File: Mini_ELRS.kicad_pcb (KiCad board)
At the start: 4 copper layers, 27.9 x 26.9 mm, 24 parts, among them J1 Conn_01x06, J2 Conn_01x06, J3 Conn_01x06, SW1 SW_Push, U1 ESP32-PICO-D4, U2 TC2014-3.3VxCTTR, U3 SX1280IMLTRT, Y1 Crystal_GND24_Small

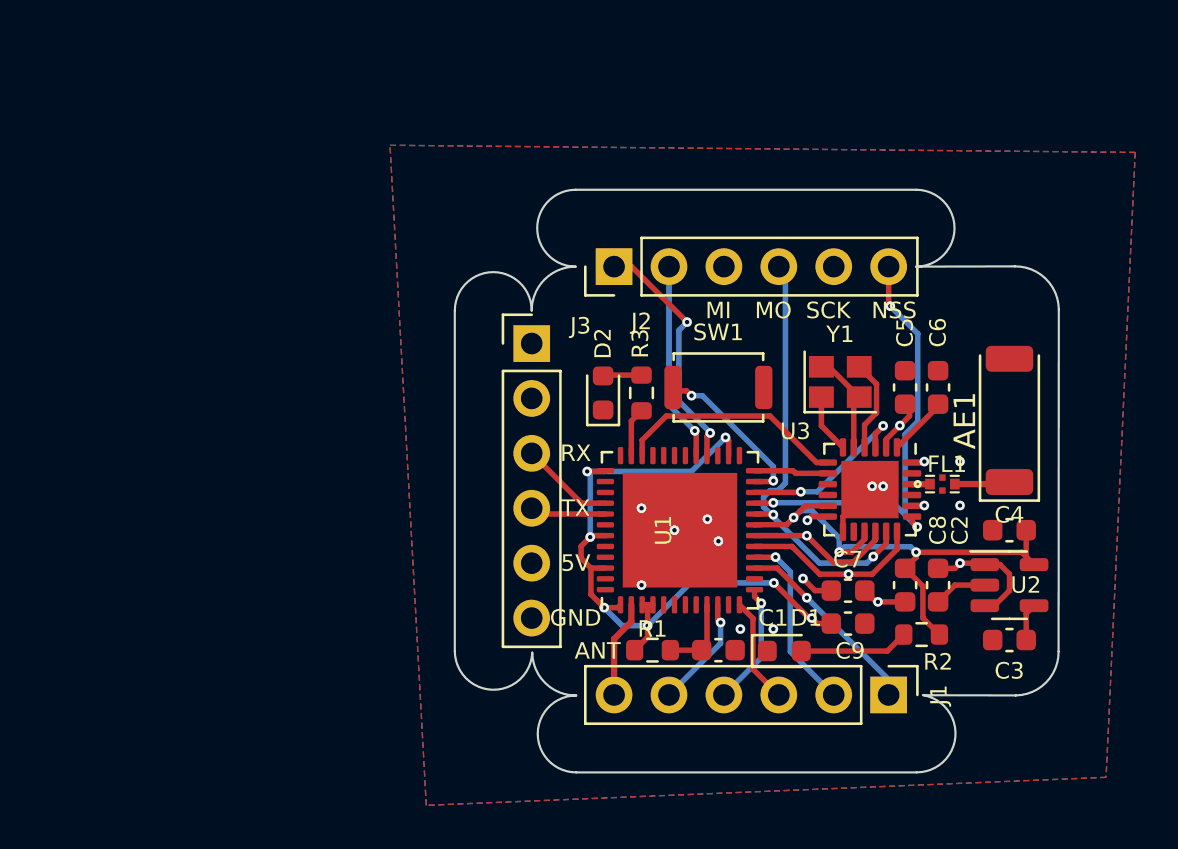
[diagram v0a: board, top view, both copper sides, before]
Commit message: remove the copper in the cutting area, which would cause the lack of connection after cutting
Signed-off-by: ncerzzk <huangzzk@bupt.edu.cn>
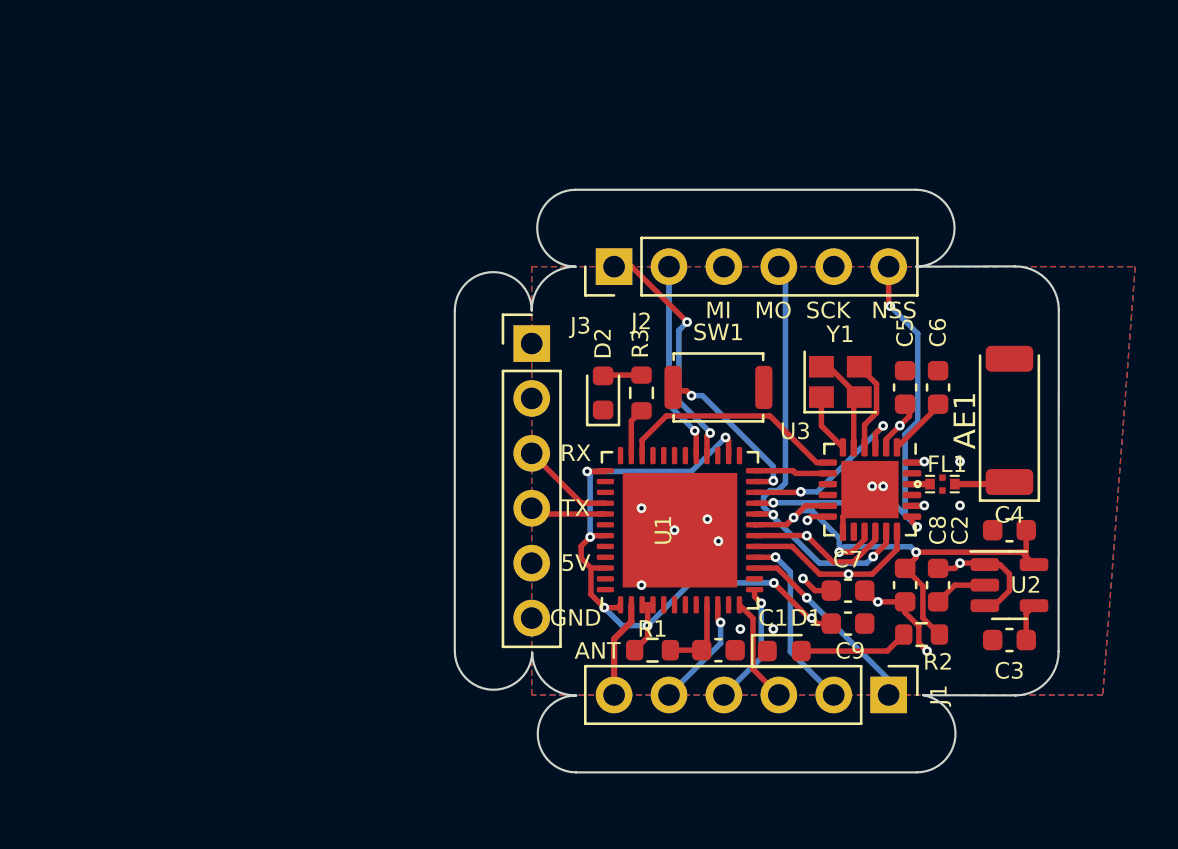
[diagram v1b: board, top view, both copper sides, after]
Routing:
- net GND: track 11.8 -> 14.5 mm, vias 14 -> 15

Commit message: stash for esp8266
Signed-off-by: ncerzzk <huangzzk@bupt.edu.cn>
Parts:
- removed D2: LED, LED_SMD:LED_0603_1608Metric
- removed J1, J2: Conn_01x06, Connector_PinHeader_2.54mm:PinHeader_1x06_P2.54mm_Vertical
- added AE2: Antenna, RF_Antenna:Texas_SWRA117D_2.4GHz_Left, F.Cu at (80.0, 61.6)
- added C10: 0.1uF, Capacitor_SMD:C_0402_1005Metric, F.Cu at (99.6, 44.7)
- added R4: NC, Resistor_SMD:R_0402_1005Metric, F.Cu at (95.6, 44.7)
- added R5: 10K, Resistor_SMD:R_0402_1005Metric, F.Cu at (119.9, 65.0)
- C1, C2, C3, C4, C5, C6, C7, C8, C9: footprint Capacitor_SMD:C_0603_1608Metric -> Capacitor_SMD:C_0402_1005Metric
- R1, R2: footprint Resistor_SMD:R_0603_1608Metric -> Resistor_SMD:R_0402_1005Metric
- R3: value 10K -> 12K; footprint Resistor_SMD:R_0603_1608Metric -> Resistor_SMD:R_0402_1005Metric
- U1: value ESP32-PICO-D4 -> ESP8266EX; footprint Package_DFN_QFN:QFN-48-1EP_7x7mm_P0.5mm_EP5.3x5.3mm -> Package_DFN_QFN:QFN-32-1EP_5x5mm_P0.5mm_EP3.45x3.45mm
- moved R3 13.1 mm to (95.6, 49.7), turned to 0 degrees
- moved C1 2.59 mm to (108.2, 68.0)
- moved R1 2.59 mm to (105.2, 68.0)
- moved D1 2.59 mm to (111.3, 68.1)
- moved U1 2.34 mm to (108.5, 63.2)
- moved C4 0.76 mm to (122.9, 65.0)
- moved SW1 0.57 mm to (108.5, 57.9)
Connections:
- R3 pad 1: Net-(D2-Pad2) -> GND
- R3 pad 2: /LED -> Net-(R3-Pad2)
- U1 pad 10: Net-(J1-Pad5) -> /MISO
- U1 pad 11: unconnected-(U1-Pad11) -> +3V3
- U1 pad 12: Net-(J1-Pad3) -> /MOSI
- U1 pad 13: Net-(J1-Pad4) -> /NSS
- U1 pad 14: unconnected-(U1-Pad14) -> Net-(R4-Pad1)
- U1 pad 15: Net-(J1-Pad1) -> Net-(SW1-Pad1)
- U1 pad 16: Net-(J1-Pad2) -> /NRST
- U1 pad 17: /SCK -> +3V3
- U1 pad 18: /MISO -> unconnected-(U1-Pad18)
- U1 pad 19: +3V3 -> unconnected-(U1-Pad19)
- U1 pad 2: /ESP32_ANT -> Net-(U1-Pad2)
- U1 pad 20: /MOSI -> unconnected-(U1-Pad20)
- U1 pad 21: /NSS -> unconnected-(U1-Pad21)
- U1 pad 22: /NRST -> unconnected-(U1-Pad22)
- U1 pad 23: Net-(SW1-Pad1) -> unconnected-(U1-Pad23)
- U1 pad 24: /DIO1 -> /BUSY
- U1 pad 25: unconnected-(U1-Pad25) -> /RX
- U1 pad 26: +3V3 -> /TX
- U1 pad 28: Net-(J2-Pad1) -> unconnected-(U1-Pad28)
- U1 pad 29: Net-(J2-Pad2) -> +3V3
- U1 pad 30: unconnected-(U1-Pad30) -> +3V3
- U1 pad 31: unconnected-(U1-Pad31) -> Net-(R3-Pad2)
- U1 pad 33: unconnected-(U1-Pad33) -> GND
- U1 pad 5: unconnected-(U1-Pad5) -> Net-(C10-Pad2)
- U1 pad 7: unconnected-(U1-Pad7) -> Net-(C1-Pad1)
- U1 pad 9: Net-(C1-Pad1) -> /SCK
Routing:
- net +3V3: track 61.2 -> 0.00 mm, vias 10 -> 0
- net +5V: track 28.5 -> 0.00 mm, vias 1 -> 0
- net /SCK: track 27.3 -> 0.00 mm, vias 1 -> 0
- net /NSS: track 21.6 -> 0.00 mm, vias 3 -> 0
- net /MISO: track 21.6 -> 0.00 mm, vias 1 -> 0
- net /MOSI: track 20.5 -> 0.00 mm, vias 2 -> 0
- net GND: track 14.5 -> 0.00 mm, vias 15 -> 0
- net Net-(C5-Pad1): track 14.4 -> 0.00 mm, vias 3 -> 0
- net Net-(J2-Pad1): track 11.4 -> 0.00 mm, vias 2 -> 0
- net /BUSY: track 10.7 -> 0.00 mm
- net Net-(J2-Pad2): track 9.26 -> 0.00 mm, vias 1 -> 0
- net Net-(J1-Pad1): track 9.05 -> 0.00 mm, vias 1 -> 0
- net Net-(J1-Pad2): track 8.46 -> 0.00 mm, vias 1 -> 0
- net /NRST: track 8.37 -> 0.00 mm, vias 2 -> 0
- net Net-(SW1-Pad1): track 7.56 -> 0.00 mm, vias 2 -> 0
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
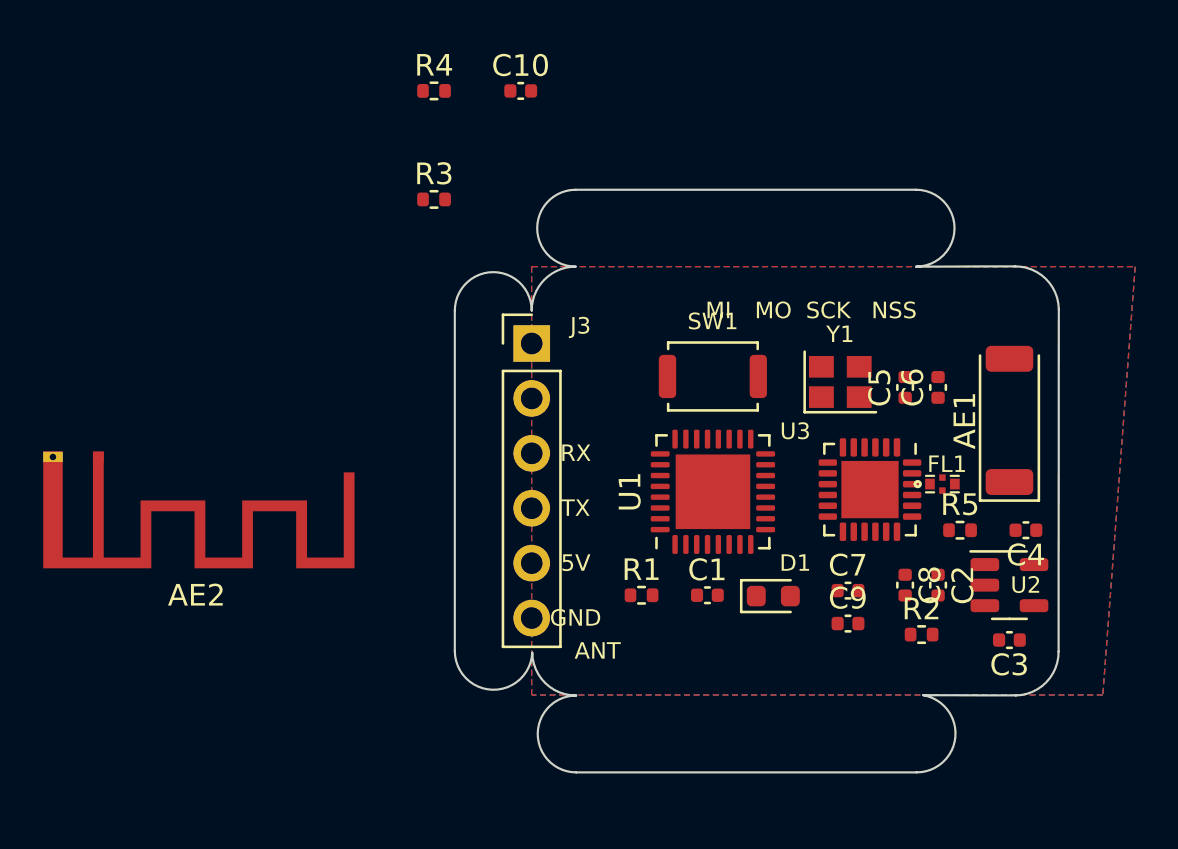
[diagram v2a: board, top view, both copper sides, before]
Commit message: update esp8266 v0.7
Signed-off-by: ncerzzk <huangzzk@bupt.edu.cn>
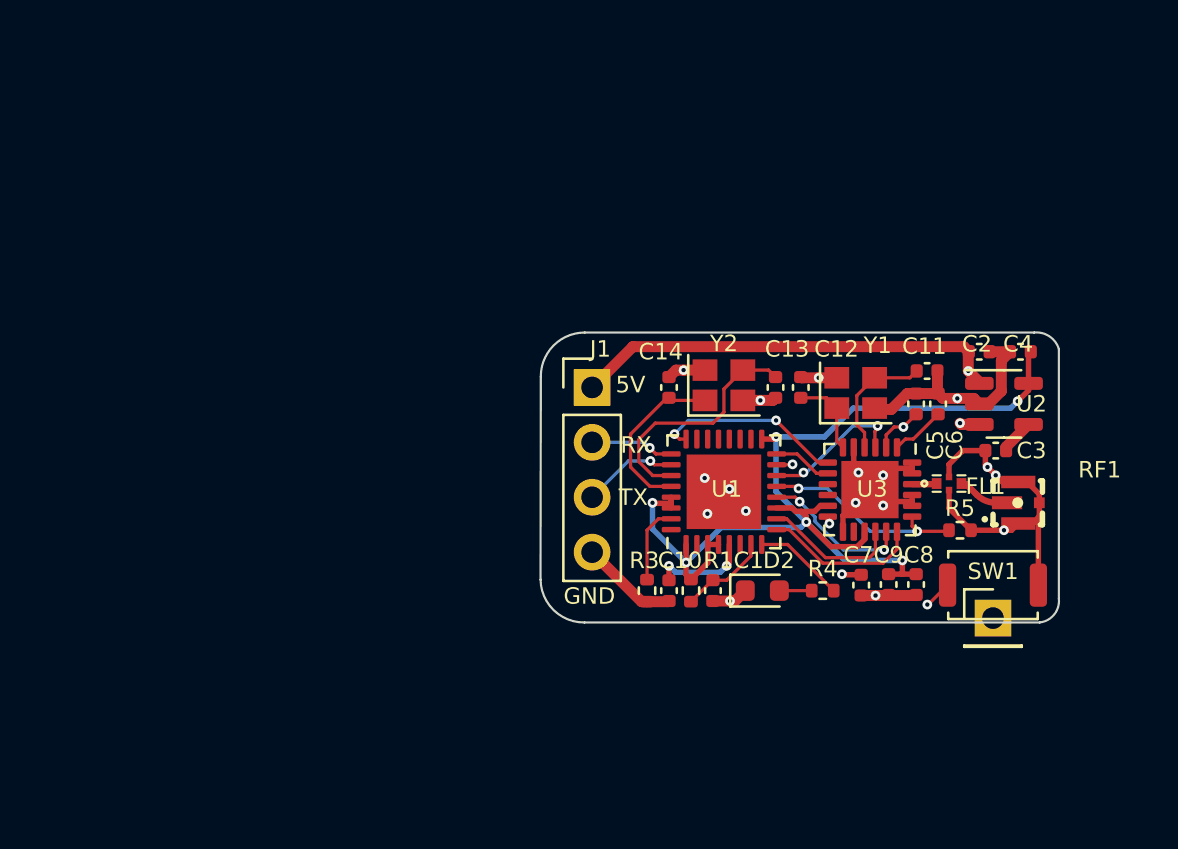
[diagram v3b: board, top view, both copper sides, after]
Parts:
- removed AE1: Antenna, RF_Antenna:Johanson_2450AT43F0100
- removed AE2: Antenna, RF_Antenna:Texas_SWRA117D_2.4GHz_Left
- removed D1: LED, LED_SMD:LED_0603_1608Metric
- removed J3: Conn_01x06, Connector_PinHeader_2.54mm:PinHeader_1x06_P2.54mm_Vertical
- removed R2: 10K, Resistor_SMD:R_0402_1005Metric
- added C11: NC, Capacitor_SMD:C_0402_1005Metric, F.Cu at (118.4, 57.7)
- added C12: NC, Capacitor_SMD:C_0402_1005Metric, F.Cu at (112.5, 58.4)
- added C13: NC, Capacitor_SMD:C_0402_1005Metric, F.Cu at (111.4, 58.4)
- added C14: NC, Capacitor_SMD:C_0402_1005Metric, F.Cu at (106.4, 58.4)
- added D2: LED, LED_SMD:LED_0603_1608Metric, F.Cu at (110.7, 67.8)
- added J1: Conn_01x04, Connector_PinHeader_2.54mm:PinHeader_1x04_P2.54mm_Vertical, F.Cu at (102.9, 58.4)
- added REF**: PinHeader_1x01_P2.54mm_Vertical, Connector_PinHeader_2.54mm:PinHeader_1x01_P2.54mm_Vertical, F.Cu at (121.4, 69.1)
- added RF1: KH-IPEX4-2020, kicad_lceda:IPEX4-SMD_4P-L1.8-W1.7-LS2.0-L_KH-IPEX4-2020, F.Cu at (122.8, 63.8)
- added Y2: Crystal_GND24_Small, Crystal:Crystal_SMD_2520-4Pin_2.5x2.0mm, F.Cu at (109.0, 58.3)
- R4: value NC -> 10K
- moved R4 29.3 mm to (113.5, 67.8)
- moved C10 24.1 mm to (106.4, 67.8), turned to 90 degrees
- moved R3 20.6 mm to (105.4, 67.8), turned to 90 degrees
- moved SW1 16.2 mm to (121.4, 67.6)
- moved C2 11.0 mm to (120.8, 56.8), turned to 0 degrees
- moved C3 8.79 mm to (121.5, 61.3)
- moved U2 8.39 mm to (121.9, 59.2)
- moved C4 8.26 mm to (122.7, 56.8)
- moved C9 2.61 mm to (116.6, 67.5), turned to -90 degrees
- moved R1 2.30 mm to (107.4, 67.8), turned to -90 degrees
- moved C5 0.92 mm to (117.9, 59.2)
- moved Y1 0.87 mm to (115.1, 58.7)
- moved C6 0.76 mm to (118.9, 59.2)
- moved C7 0.66 mm to (115.3, 67.6), turned to -90 degrees
- moved C8 0.51 mm to (117.9, 67.5)
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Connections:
- FL1 pad 3: Net-(AE1-Pad1) -> /RFOUT
- R4 pad 1: Net-(R4-Pad1) -> Net-(D2-Pad2)
- R4 pad 2: /DIO1 -> /LED
- U1 pad 14: Net-(R4-Pad1) -> /NRST
- U1 pad 16: /NRST -> /DIO1
- U1 pad 2: Net-(U1-Pad2) -> unconnected-(U1-Pad2)
- U1 pad 27: unconnected-(U1-Pad27) -> Net-(U1-Pad27)
- U1 pad 28: unconnected-(U1-Pad28) -> Net-(U1-Pad28)
- U1 pad 8: unconnected-(U1-Pad8) -> /LED
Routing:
- net +3V3: track 0.00 -> 48.6 mm, vias 0 -> 6
- net GND: track 0.00 -> 46.3 mm, vias 0 -> 17
- net +5V: track 0.00 -> 23.5 mm, vias 0 -> 2
- net Net-(SW1-Pad1): track 0.00 -> 13.8 mm, vias 0 -> 2
- net Net-(C5-Pad1): track 0.00 -> 13.7 mm, vias 0 -> 3
- net Net-(U1-Pad27): track 0.00 -> 11.2 mm
- net /NSS: track 0.00 -> 9.56 mm, vias 0 -> 2
- net /BUSY: track 0.00 -> 8.79 mm, vias 0 -> 2
- net Net-(U1-Pad28): track 0.00 -> 7.86 mm
- net /SCK: track 0.00 -> 7.29 mm
- net /MOSI: track 0.00 -> 6.99 mm, vias 0 -> 2
- net /NRST: track 0.00 -> 6.65 mm, vias 0 -> 2
- net /MISO: track 0.00 -> 6.35 mm
- net Net-(U3-Pad4): track 0.00 -> 5.79 mm
- net Net-(C10-Pad2): track 0.00 -> 4.62 mm, vias 0 -> 2
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- removed copper zone on B.Cu, net GND
- removed copper zone on F.Cu, net GND
- removed copper zone on In2.Cu, net GND
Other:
- board size 27.9 x 26.9 mm -> 24 x 13.4 mm
- board text removed: "ANT"
- board text removed: "MI"
- board text removed: "MO"
- board text removed: "NSS"
- board text removed: "SCK"

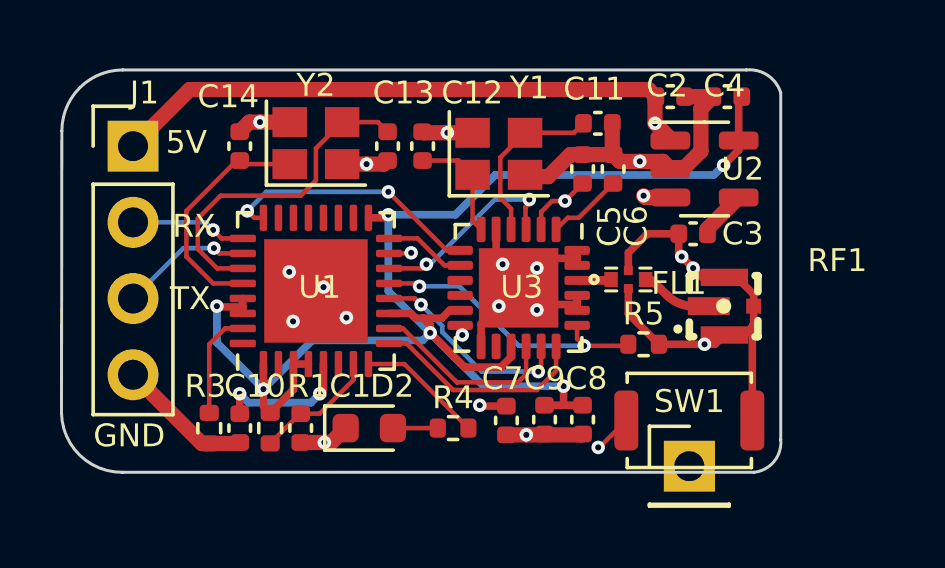
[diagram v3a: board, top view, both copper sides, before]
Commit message: remove some unnecessary cap/res, remove ipex4.0 , add esp8266 lna
Signed-off-by: huangzzk <huangcmzzk@gmail.com>
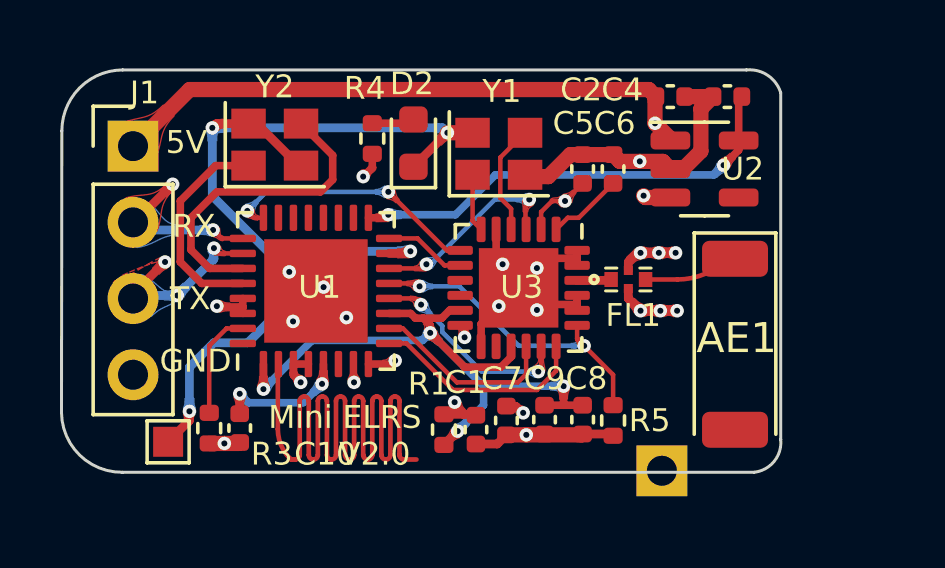
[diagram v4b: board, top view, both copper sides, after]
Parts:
- removed C11, C12, C13, C14: NC, Capacitor_SMD:C_0402_1005Metric
- removed C3: 180pF, Capacitor_SMD:C_0402_1005Metric
- removed REF**: PinHeader_1x01_P2.54mm_Vertical, Connector_PinHeader_2.54mm:PinHeader_1x01_P2.54mm_Vertical
- removed RF1: KH-IPEX4-2020, kicad_lceda:IPEX4-SMD_4P-L1.8-W1.7-LS2.0-L_KH-IPEX4-2020
- removed SW1: SW_Push, Button_Switch_SMD:SW_Push_SPST_NO_Alps_SKRK
- added ?: , , F.Cu at (120.5, 69.2)
- added AE1: Antenna, RF_Antenna:Johanson_2450AT43F0100, F.Cu at (122.9, 65.0)
- added TP1: TestPoint, TestPoint:TestPoint_Pad_1.0x1.0mm, F.Cu at (104.0, 68.3)
- Y1, Y2: value Crystal_GND24_Small -> 52M
- moved R4 10.0 mm to (110.8, 58.2), turned to -90 degrees
- moved D2 9.61 mm to (112.2, 58.3), turned to 90 degrees
- moved C1 5.84 mm to (114.3, 67.9)
- moved R1 5.79 mm to (113.2, 67.9), turned to 90 degrees
- moved R5 2.74 mm to (118.9, 67.6), turned to -90 degrees
- moved Y2 1.37 mm to (107.6, 58.4)
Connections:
- U2 pad 4: Net-(C3-Pad1) -> unconnected-(U2-Pad4)
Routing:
- net unconnected-(U1-Pad2): track 0.00 -> 31.0 mm
- net /LED: track 4.22 -> 8.40 mm, vias 0 -> 2
- net +3V3: track 48.6 -> 51.3 mm, vias 6 -> 8
- net Net-(U3-Pad4): track 5.79 -> 3.71 mm
- net Net-(C1-Pad1): track 4.15 -> 6.06 mm, vias 0 -> 2
- net /TX: track 4.43 -> 6.30 mm, vias 1 -> 3
- net Net-(U3-Pad6): track 3.80 -> 1.94 mm
- net /RX: track 3.88 -> 5.73 mm, vias 1 -> 2
- net Net-(C3-Pad1): track 1.64 -> 0.00 mm
- net Net-(U1-Pad15): track 13.8 -> 12.5 mm
- net /NSS: track 9.56 -> 10.9 mm
- net GND: track 46.3 -> 45.1 mm, vias 17 -> 19
- net /RFOUT: track 1.89 -> 2.90 mm
- net Net-(U1-Pad27): track 11.2 -> 10.6 mm
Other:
- board text added: "Mini ELRS V2.0"
